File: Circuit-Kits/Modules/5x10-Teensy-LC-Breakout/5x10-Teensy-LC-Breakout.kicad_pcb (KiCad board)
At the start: 2 copper layers, 39.8 x 79.8 mm, 2 parts, among them U1 Teensy

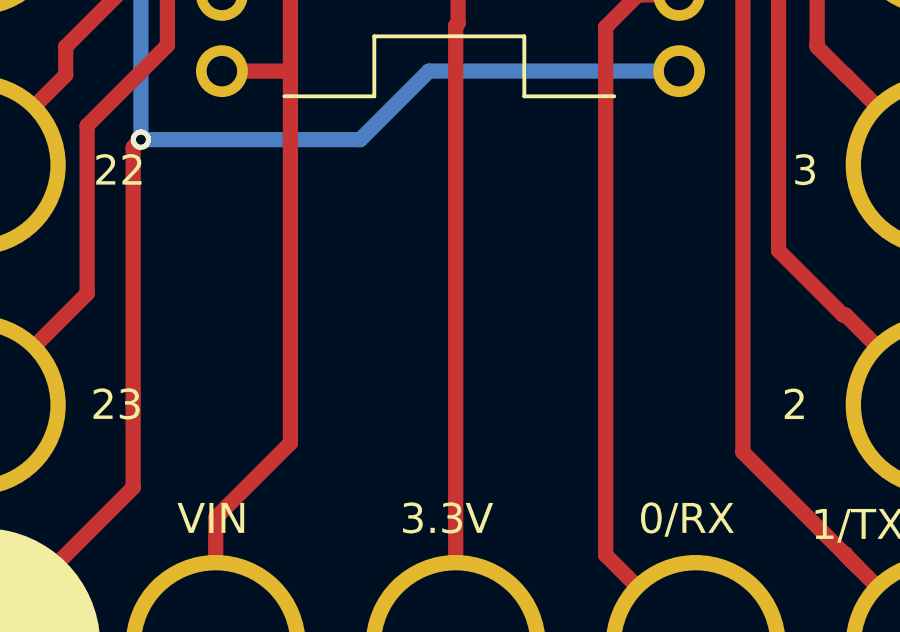
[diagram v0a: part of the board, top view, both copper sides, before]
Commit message: Release v1.3 5x10 Teensy Touch Board.
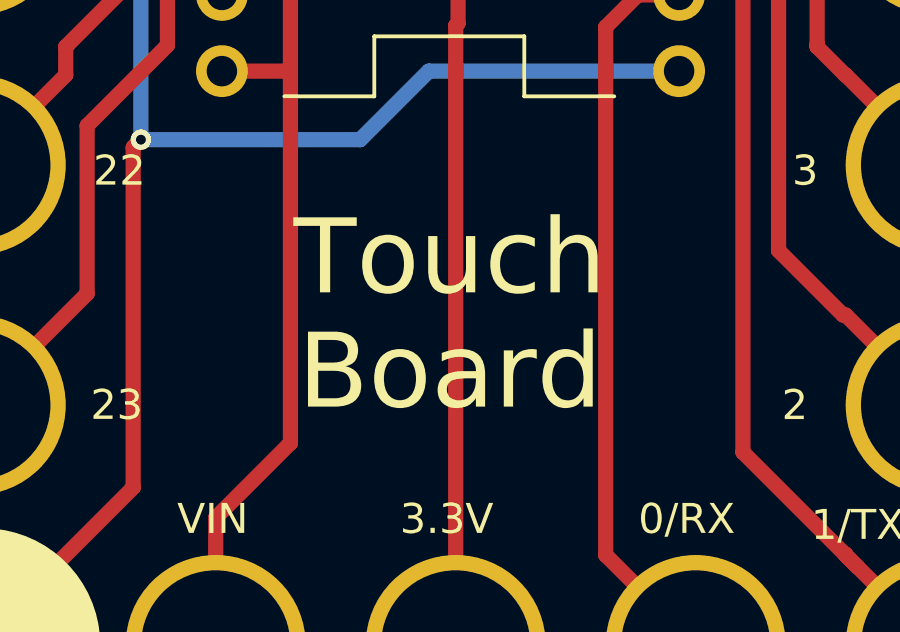
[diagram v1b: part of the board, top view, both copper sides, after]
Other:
- board text added: "Board"
- board text added: "Touch"
- board text added: "v1.3"
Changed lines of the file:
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@@
     (area 19.532959 58.405039 220.670359 139.70836)
     (thickness 1.6)
-    (drawings 3)
+    (drawings 6)
     (tracks 114)
     (zones 0)
@@
     (title "5x10 Teensy LC Breakout Module")
     (date "20 Jan 2017")
-    (rev v1.2)
+    (rev v1.3)
     (company "All rights reserved.")
     (comment 1 help@browndoggadgets.com)
@@
     (pad 1/TX thru_hole circle (at 32 48 90) (size 6 6) (drill 4.98) (layers *.Cu *.Mask))
   )
+  (gr_text Board (at 39.624 125.476) (layer F.SilkS)
+    (effects (font (size 2.5 2.5) (thickness 0.4)))
+  )
+  (gr_text v1.3 (at 39.624 123.444) (layer B.SilkS)
+    (effects (font (size 2 2) (thickness 0.3)) (justify mirror))
+  )
+  (gr_text Touch (at 39.624 121.666) (layer F.SilkS)
+    (effects (font (size 2.5 2.5) (thickness 0.4)))
+  )
   (gr_text "FABRICATION NOTES\n\n1. THIS IS A 2 LAYER BOARD. \n2. EXTERNAL LAYERS SHALL HAVE 1 OZ COPPER.\n3. MATERIAL: FR4 AND 0.062 INCH +/- 10% THICK.\n4. BOARDS SHALL BE ROHS COMPLIANT. \n5. MANUFACTURE IN ACCORDANCE WITH IPC-6012 CLASS 2\n6. MASK: BOTH SIDES OF THE BOARD SHALL HAVE \n   SOLDER MASK (GREEN) OVER BARE COPPER. \n7. SILK: BOTH SIDES OF THE BOARD SHALL HAVE WHITE SILK. \n   DO NOT PLACE SILK OVER BARE COPPER.\n8. FINISH: ENIG.\n9. MINIMUM TRACE WIDTH - 0.006 INCH.\n   MINIMUM SPACE - 0.006 INCH.\n   MINIMUM HOLE DIA - 0.013 INCH. \n10. MAX HOLE PLACEMENT TOLERANCE OF +/- 0.003 INCH.\n11. MAX HOLE DIAMETER TOLERANCE OF +/- 0.003 INCH AFTER PLATING." (at 77.8256 97.6884) (layer Dwgs.User)

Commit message: Release v1.4 5x10 Teensy LC
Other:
- board text added: "Inventor"
- board text added: "v1.4"
- board text removed: "Touch"
- board text removed: "v1.3"
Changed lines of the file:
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@@
-(kicad_pcb (version 4) (host pcbnew 4.0.5-e0-6337~49~ubuntu16.04.1)
+(kicad_pcb (version 4) (host pcbnew 4.0.7-e2-6376~58~ubuntu16.04.1)
   (general
     (links 0)
@@
     (title "5x10 Teensy LC Breakout Module")
     (date "20 Jan 2017")
-    (rev v1.3)
+    (rev "v1.4")
     (company "All rights reserved.")
-    (comment 1 help@browndoggadgets.com)
-    (comment 2 http://browndoggadgets.com/)
+    (comment 1 "help@browndoggadgets.com")
+    (comment 2 "http://browndoggadgets.com/")
     (comment 3 "Brown Dog Gadgets")
   )
@@
     (effects (font (size 2.5 2.5) (thickness 0.4)))
   )
-  (gr_text v1.3 (at 39.624 123.444) (layer B.SilkS)
+  (gr_text v1.4 (at 39.624 123.444) (layer B.SilkS)
     (effects (font (size 2 2) (thickness 0.3)) (justify mirror))
   )
-  (gr_text Touch (at 39.624 121.666) (layer F.SilkS)
+  (gr_text Inventor (at 39.624 121.666) (layer F.SilkS)
     (effects (font (size 2.5 2.5) (thickness 0.4)))
   )

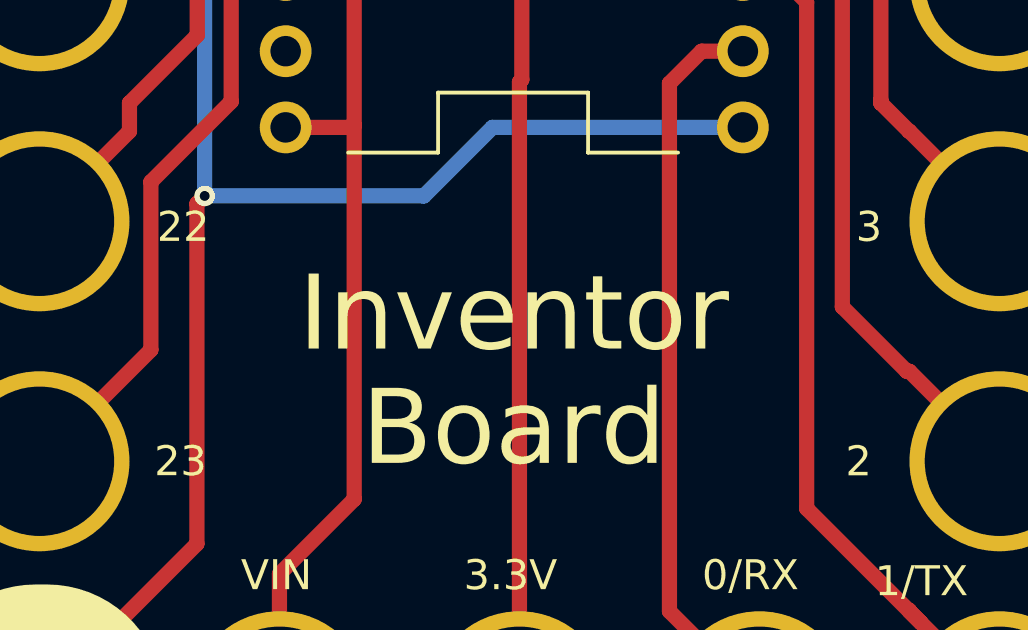
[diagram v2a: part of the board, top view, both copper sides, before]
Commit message: Silk say Invention. No ver change.
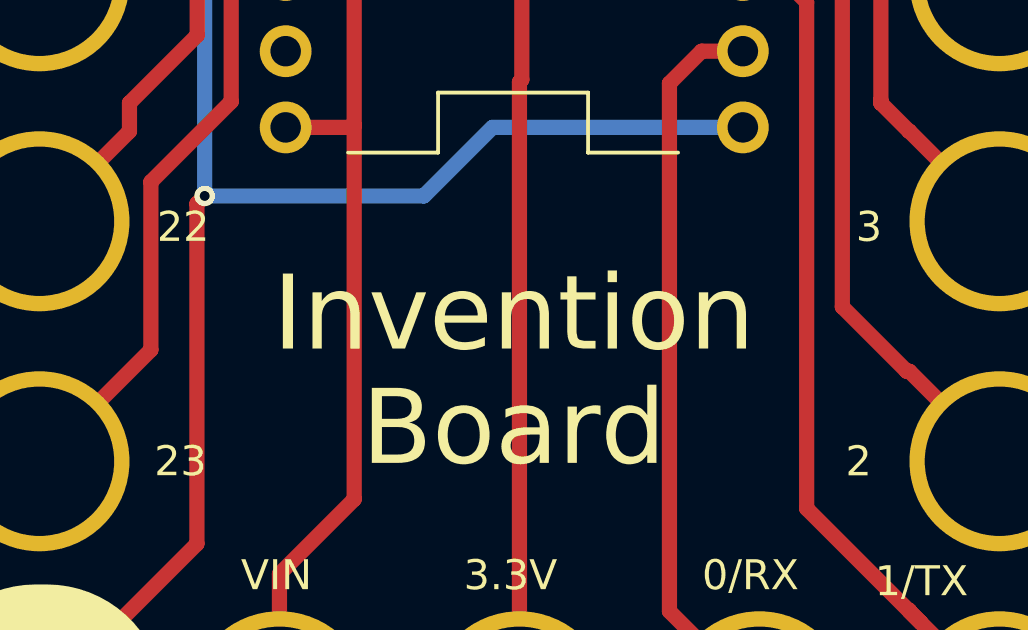
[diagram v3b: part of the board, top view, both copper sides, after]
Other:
- board text added: "Invention"
- board text removed: "Inventor"
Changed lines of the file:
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@@
     (title "5x10 Teensy LC Breakout Module")
     (date "20 Jan 2017")
-    (rev "v1.4")
+    (rev v1.4)
     (company "All rights reserved.")
-    (comment 1 "help@browndoggadgets.com")
-    (comment 2 "http://browndoggadgets.com/")
+    (comment 1 help@browndoggadgets.com)
+    (comment 2 http://browndoggadgets.com/)
     (comment 3 "Brown Dog Gadgets")
   )
@@
     (effects (font (size 2 2) (thickness 0.3)) (justify mirror))
   )
-  (gr_text Inventor (at 39.624 121.666) (layer F.SilkS)
+  (gr_text Invention (at 39.624 121.666) (layer F.SilkS)
     (effects (font (size 2.5 2.5) (thickness 0.4)))
   )
